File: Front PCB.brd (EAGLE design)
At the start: 85.9 x 53.3 mm, 10 parts

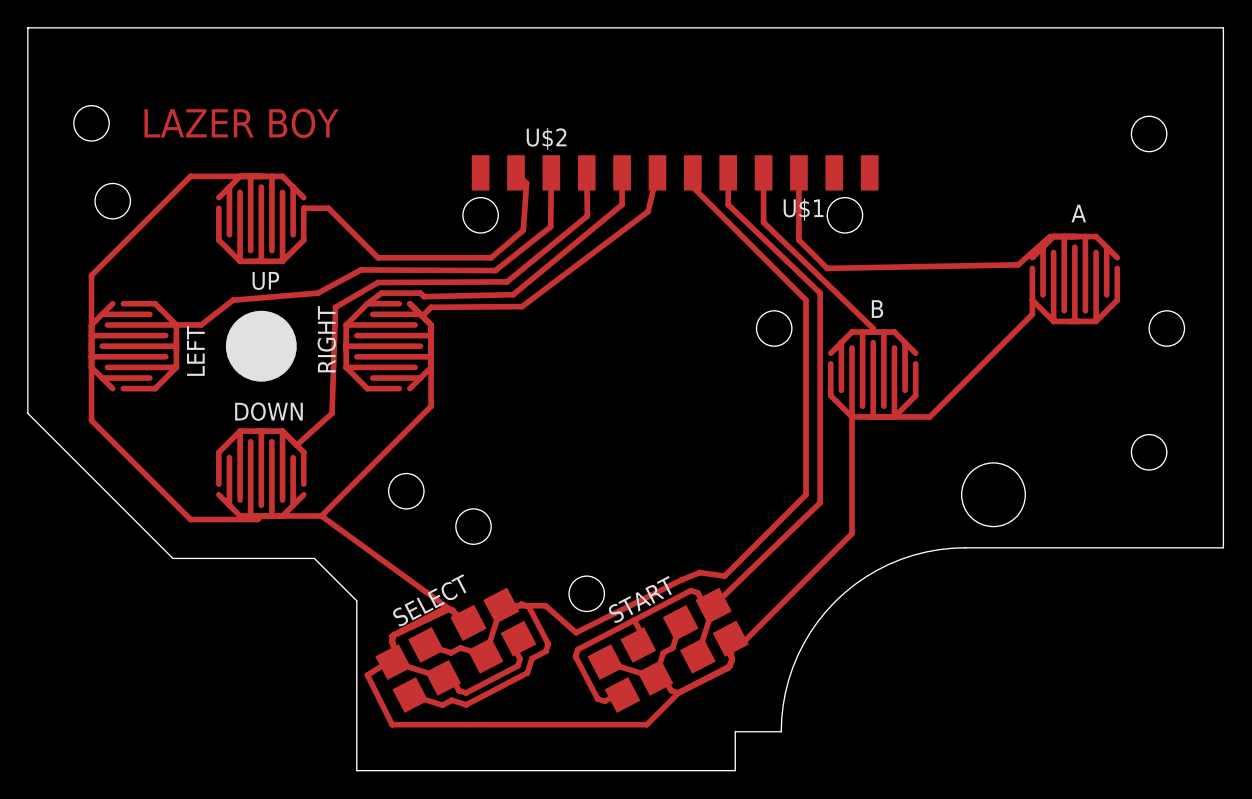
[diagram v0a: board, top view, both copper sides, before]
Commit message: Redesign board to use through-hole pins
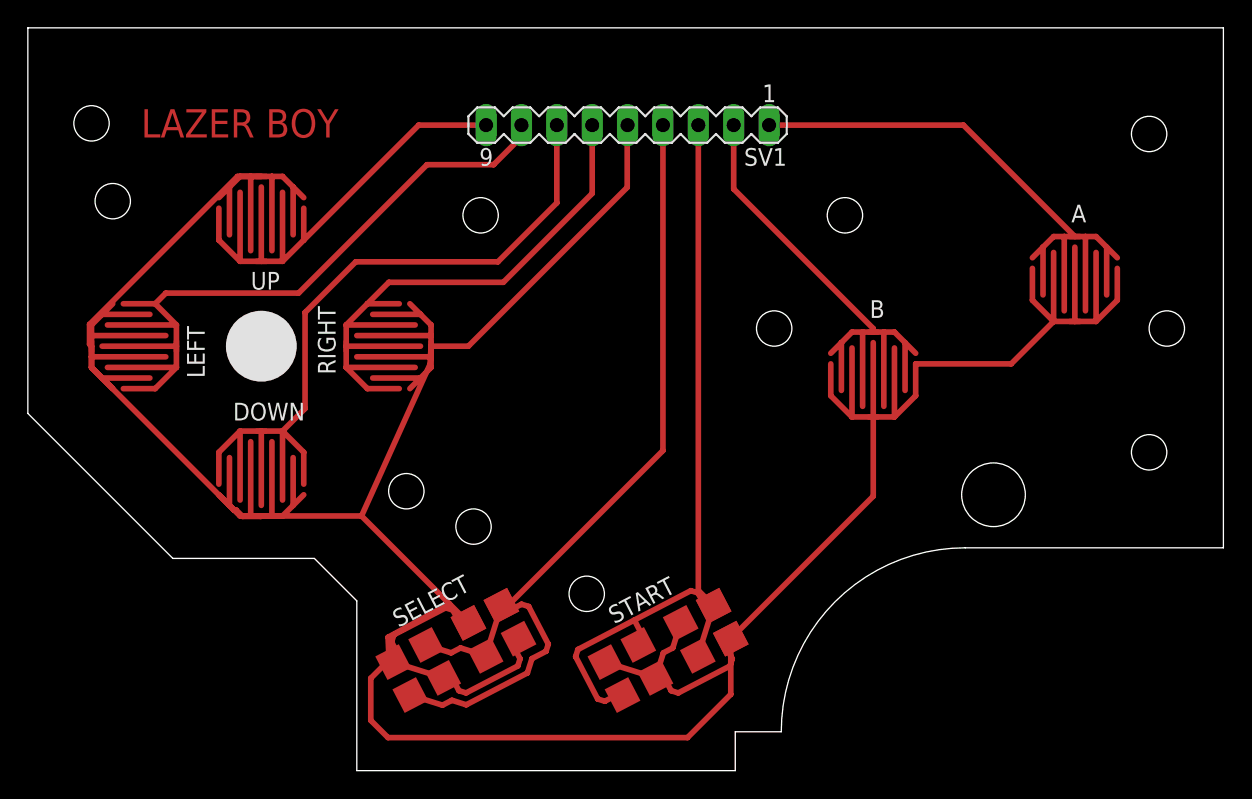
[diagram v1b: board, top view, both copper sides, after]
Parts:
- removed U$1, U$2: FTDI-SMD-HEADER, fab:1X06SMD
- added SV1: (no value), con-lstb:MA09-1
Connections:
- net A: now also SV1.1; no longer U$1.4
- net B: now also SV1.2; no longer U$1.3
- net DOWN: now also SV1.7; no longer U$2.3
- net GND: now also SV1.5; no longer U$2.1
- net LEFT: now also SV1.8; no longer U$2.4
- net RIGHT: now also SV1.6; no longer U$2.2
- net SEL: now also SV1.4; no longer U$1.1
- net START: now also SV1.3; no longer U$1.2
- net UP: now also SV1.9; no longer U$2.5
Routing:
- net SEL: track 52.5 -> 39.6 mm
- net GND: track 175.8 -> 165.9 mm
- net UP: track 22.4 -> 16.5 mm
- net B: track 14.8 -> 19.0 mm
- net START: track 37.1 -> 35.0 mm
- net RIGHT: track 23.3 -> 24.3 mm
- net A: track 26.3 -> 25.3 mm
- net LEFT: track 32.9 -> 32.1 mm

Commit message: Crop slightly on top
To avoid collisions with the screen I'm using. Longer forehead was
necessary when there were horizontal headers sticking out.
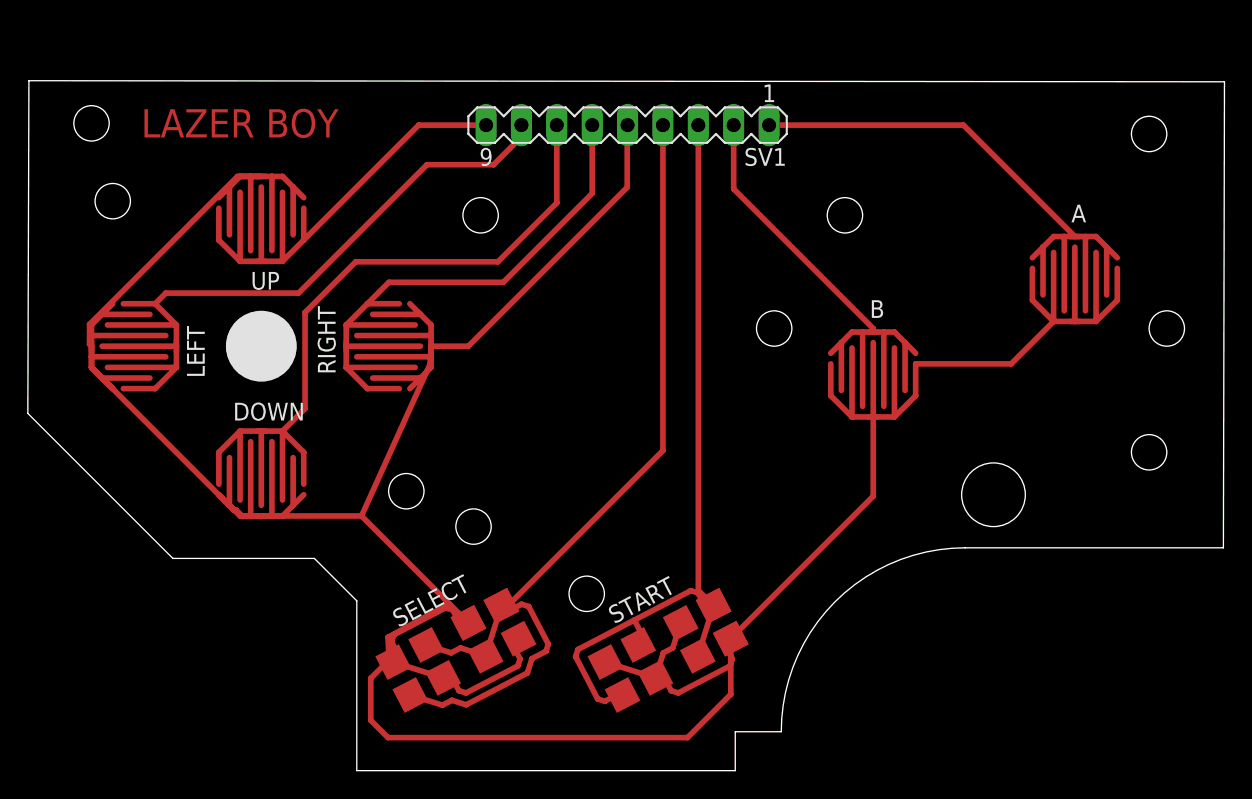
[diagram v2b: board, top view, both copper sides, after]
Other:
- board size 85.9 x 53.3 mm -> 85.9 x 49.5 mm
